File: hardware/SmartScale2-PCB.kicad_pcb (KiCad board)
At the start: 4 copper layers, 42 parts, among them J1 Conn_ARM_JTAG_SWD_10, J2 USB_C_Receptacle_USB2.0_16P, J3 Conn_01x02, J4 Conn_01x06, J5 Conn_01x03_MountingPin, J6 Conn_01x04_MountingPin, Q1 MMBT4403, SW1 SW_Push_JTP-1130, U1 ESP32-C6-WROOM-1, U2 MCP73831-2-OT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

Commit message: PCB rough layout
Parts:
- added L2: L, Inductor_SMD:L_0805_2012Metric_Pad1.05x1.20mm_HandSolder, F.Cu at (45.4, 53.0)
- R12: value R -> 10k
- moved JP1 94.8 mm to (49.5, 50.0), turned to 180 degrees
- moved C11 93.2 mm to (43.2, 53.0), turned to -90 degrees
- moved R10 90.7 mm to (61.2, 61.8)
- moved R11 90.6 mm to (61.2, 63.8)
- moved C12 89.8 mm to (60.2, 55.5)
- moved R8 89.3 mm to (44.8, 63.4)
- moved R9 89.3 mm to (44.8, 60.8)
- moved U3 89.2 mm to (55.1, 58.7)
- moved C10 88.5 mm to (50.1, 62.5)
- moved R6 87.8 mm to (49.4, 57.4)
- moved C9 87.3 mm to (55.1, 65.0)
- moved Q1 87.2 mm to (48.8, 54.5)
- moved J5 85.0 mm to (40.6, 82.2), turned to -90 degrees
- moved JP2 84.5 mm to (63.0, 55.5), turned to -90 degrees
- moved J4 84.4 mm to (38.4, 52.0)
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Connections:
- net Net-(Q1-C) renamed /Q1_C
- J4 pad 3: /A+ -> /A-
- J4 pad 4: /A- -> /A+
- J4 pad 5: /B+ -> /B-
- J4 pad 6: /B- -> /B+
- JP1 pad 1: Net-(JP1-A) -> /Q1_E
- Q1 pad 1: Net-(JP1-A) -> /Q1_B
- Q1 pad 2: Net-(Q1-B) -> /Q1_E
- U1 pad 26: unconnected-(U1-GPIO3/ADC1_CH3-Pad26) -> /T2
- U1 pad 27: unconnected-(U1-GPIO2/ADC1_CH2-Pad27) -> /T1
- U3 pad 1: Net-(JP1-A) -> /Q1_E
- U3 pad 2: Net-(Q1-B) -> /Q1_B
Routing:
- net /B+: track 0.00 -> 29.8 mm
- net /B-: track 0.00 -> 26.6 mm
- net GND: track 0.00 -> 17.5 mm
- net /Q1_C: track 0.00 -> 10.3 mm
- net Net-(U3-INA-): track 0.00 -> 7.29 mm
- net Net-(U3-VFB): track 0.00 -> 7.17 mm
- net Net-(U3-INA+): track 0.00 -> 7.10 mm
- net /A-: track 0.00 -> 7.00 mm
- net /A+: track 0.00 -> 7.00 mm
- net /E+: track 0.00 -> 6.80 mm
- net /RX0: track 0.00 -> 6.74 mm
- net VCC: track 0.00 -> 5.65 mm
- net Net-(U3-VBG): track 0.00 -> 5.61 mm
- net Net-(JP2-C): track 0.00 -> 5.41 mm
- net /Q1_E: track 0.00 -> 3.20 mm
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- added copper zone on In1.Cu, net GND
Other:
- board outline added: 40 x 50 mm
- board text added: "${TITLE} @Jannled"
- board text added: "A+"
- board text added: "A-"
- board text added: "B+"
- board text added: "B-"
- board text added: "E+"
- board text added: "E-"
- board text added: "UART"

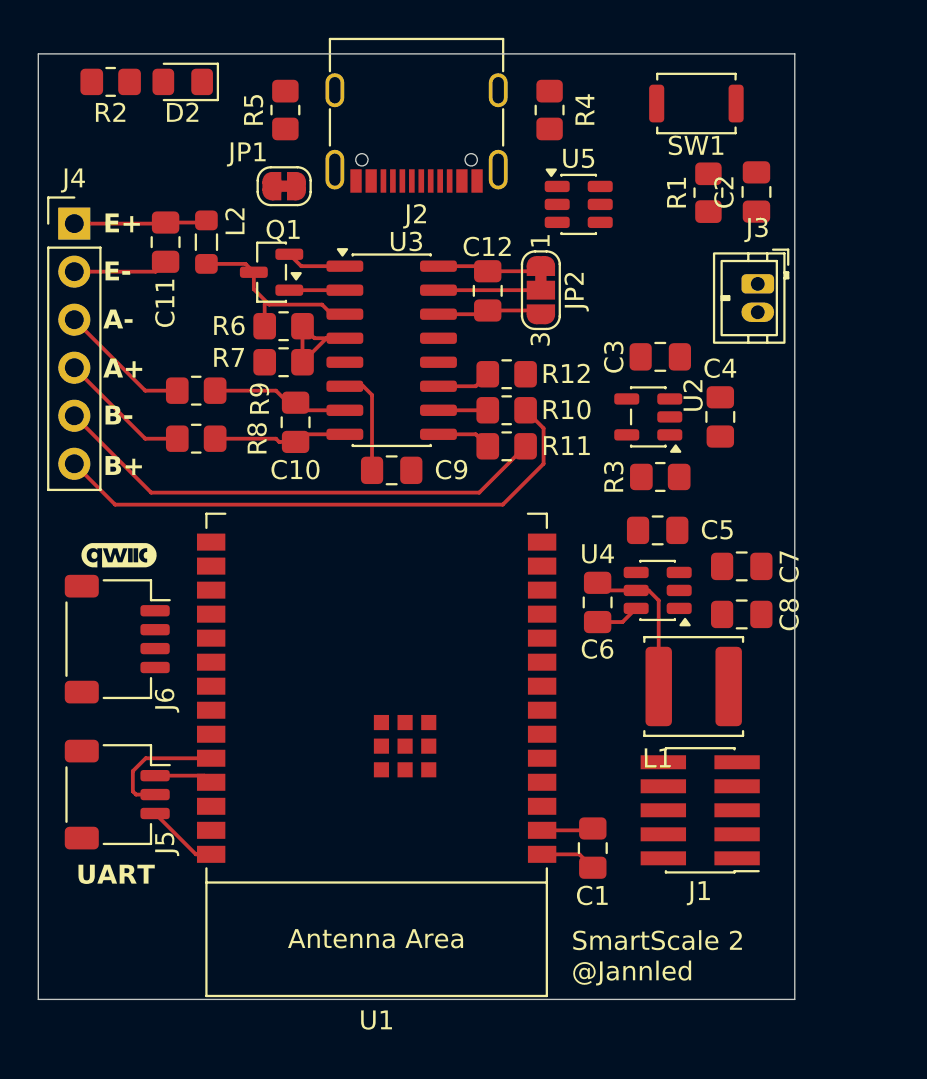
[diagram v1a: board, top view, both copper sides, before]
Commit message: Add Touch IC, continue layout
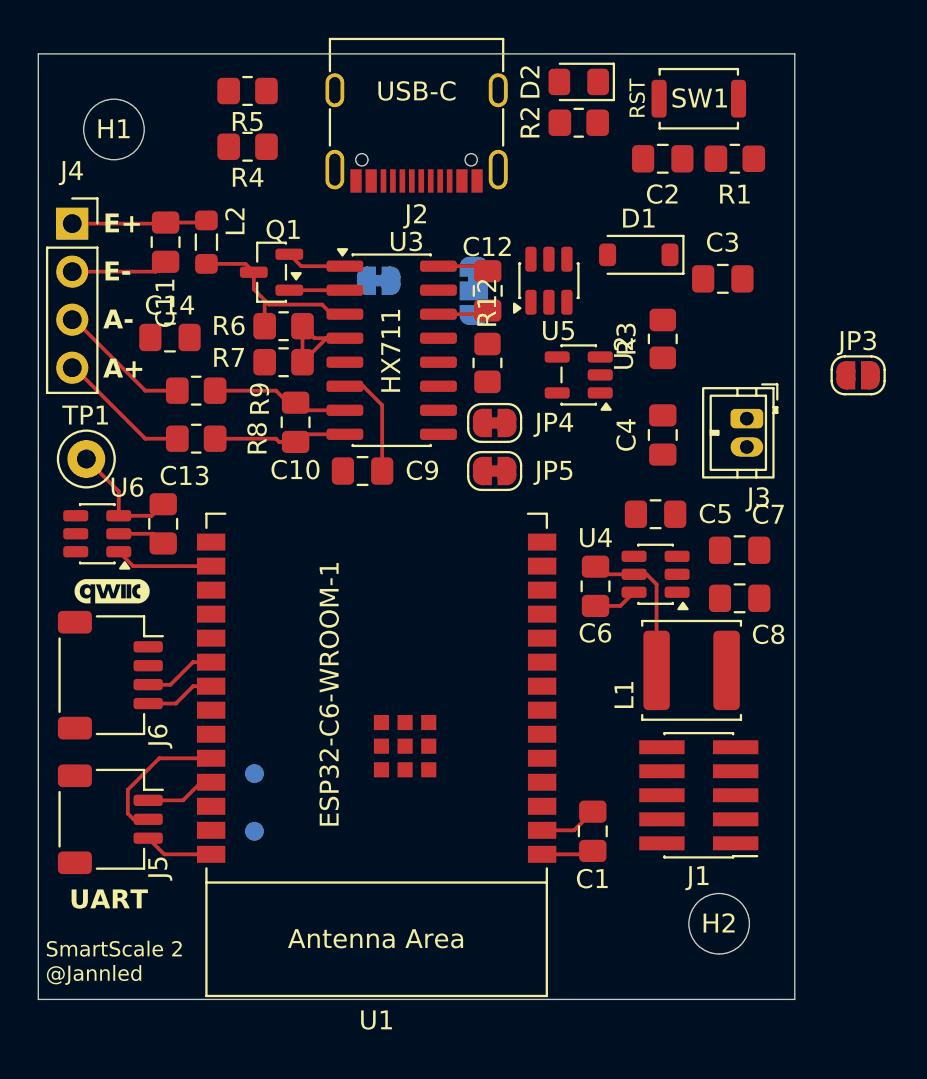
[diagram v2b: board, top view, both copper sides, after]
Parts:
- removed R10, R11: 100, Resistor_SMD:R_0805_2012Metric_Pad1.20x1.40mm_HandSolder
- added C13: 100nF, Capacitor_SMD:C_0805_2012Metric_Pad1.18x1.45mm_HandSolder, F.Cu at (43.1, 67.9)
- added C14: 10uF, Capacitor_SMD:C_0805_2012Metric_Pad1.18x1.45mm_HandSolder, F.Cu at (43.4, 58.0)
- added D1: D_Zener, Diode_SMD:D_SOD-123, F.Cu at (68.2, 53.6)
- added H1: MountingHole, MountingHole:MountingHole_3.2mm_M3_DIN965, F.Cu at (40.5, 47.0)
- added H2: MountingHole, MountingHole:MountingHole_3.2mm_M3_DIN965, F.Cu at (72.5, 89.0)
- added JP3: Jumper_2_Small_Open, Jumper:SolderJumper-2_P1.3mm_Open_RoundedPad1.0x1.5mm, F.Cu at (79.8, 60.0)
- added JP4: Jumper_2_Small_Bridged, Jumper:SolderJumper-2_P1.3mm_Bridged_RoundedPad1.0x1.5mm, F.Cu at (60.6, 62.5)
- added JP5: Jumper_2_Small_Bridged, Jumper:SolderJumper-2_P1.3mm_Bridged_RoundedPad1.0x1.5mm, F.Cu at (60.6, 65.1)
- added TP1: TestPoint, TestPoint:TestPoint_Loop_D2.50mm_Drill1.0mm, F.Cu at (39.0, 64.4)
- added TP2: TestPoint, TestPoint:TestPoint_Pad_D1.0mm, B.Cu at (47.9, 81.1)
- added TP3: TestPoint, TestPoint:TestPoint_Pad_D1.0mm, B.Cu at (47.9, 84.1)
- added U6: ~, Package_TO_SOT_SMD:SOT-23-6, F.Cu at (39.6, 68.4)
- J4: value Conn_01x06 -> Conn_01x04; footprint Connector_PinHeader_2.54mm:PinHeader_1x06_P2.54mm_Vertical -> Connector_PinSocket_2.54mm:PinSocket_1x04_P2.54mm_Vertical
- JP1, JP2: moved to B.Cu
- moved R2 24.8 mm to (65.0, 46.6)
- moved D2 20.9 mm to (65.0, 44.5)
- moved R4 16.1 mm to (47.5, 47.9), turned to 180 degrees
- moved R3 7.30 mm to (69.5, 58.1), turned to 90 degrees
- moved J3 7.15 mm to (73.9, 62.3)
- moved JP1 7.07 mm to (54.5, 55.0), turned to 0 degrees
- moved C3 5.29 mm to (72.7, 54.9)
- moved C2 5.26 mm to (69.5, 48.5), turned to 180 degrees
- moved U5 4.33 mm to (63.5, 55.0), turned to 90 degrees
- moved U2 4.30 mm to (65.0, 60.0)
- moved JP2 3.55 mm to (59.5, 55.5)
- moved C4 3.19 mm to (69.5, 63.2)
- moved R1 2.27 mm to (73.3, 48.5), turned to 180 degrees
- moved R5 2.24 mm to (47.5, 45.0), turned to 180 degrees
- moved G*** 1.94 mm to (40.4, 71.4)
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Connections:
- C2 pad 1: /EN -> /Reset
- R1 pad 2: /EN -> /Reset
- SW1 pad 2: /EN -> /Reset
- U1 pad 11: unconnected-(U1-GPIO10-Pad11) -> /HX711_DOUT
- U1 pad 12: unconnected-(U1-GPIO11-Pad12) -> /HX711_SCK
- U1 pad 16: unconnected-(U1-GPIO18-Pad16) -> /Touch
- U1 pad 20: unconnected-(U1-GPIO22-Pad20) -> /SDA
- U1 pad 21: unconnected-(U1-GPIO23-Pad21) -> /SCL
- U1 pad 26: /T2 -> Net-(U1-GPIO3/ADC1_CH3)
- U1 pad 27: /T1 -> Net-(U1-GPIO2/ADC1_CH2)
- U3 pad 10: Net-(U3-INB+) -> /B+
- U3 pad 9: Net-(U3-INB-) -> /B-
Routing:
- net /B+: track 29.8 -> 0.00 mm
- net /B-: track 26.6 -> 0.00 mm
- net Net-(U6-I): track 0.00 -> 6.31 mm
- net Net-(JP2-C): track 5.41 -> 0.00 mm
- net /Touch: track 0.00 -> 5.20 mm
- net /SDA: track 0.00 -> 3.83 mm
- net /SCL: track 0.00 -> 3.71 mm
- net VCC: track 5.65 -> 2.72 mm
- net Net-(U3-INB-): track 2.87 -> 0.00 mm
- net /HX711_SCK: track 2.87 -> 0.00 mm
- net Net-(U3-INB+): track 2.60 -> 0.00 mm
- net /RX0: track 6.74 -> 7.55 mm
- net GND: track 17.5 -> 16.7 mm
- net /TX0: track 3.11 -> 3.73 mm
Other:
- board text added: "ESP32-C6-WROOM-1"
- board text added: "HX711"
- board text added: "RST"
- board text added: "USB-C"
- board text removed: "B+"
- board text removed: "B-"

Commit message: Push from laptop
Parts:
- JP1: moved to F.Cu
- moved JP1 6.97 mm to (49.2, 50.5)
- moved R3 3.24 mm to (72.7, 57.4), turned to 180 degrees
- moved U5 1.66 mm to (64.4, 53.6)
- moved U2 0.90 mm to (65.7, 59.3)
- moved R4 0.63 mm to (47.5, 47.3)
- moved D1 0.63 mm to (68.8, 53.6), turned to -90 degrees
- moved R5 0.41 mm to (47.5, 45.4)
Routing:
- net /MTDO: track 0.00 -> 13.1 mm
- net /MTCK: track 0.00 -> 12.1 mm, vias 0 -> 2
- net VCC: track 2.72 -> 12.1 mm
- net /MTMS: track 0.00 -> 8.49 mm
- net /MTDI: track 0.00 -> 6.62 mm
- net /Q1_E: track 3.20 -> 6.84 mm
- net /B-: track 0.00 -> 3.12 mm
- net /B+: track 0.00 -> 2.60 mm

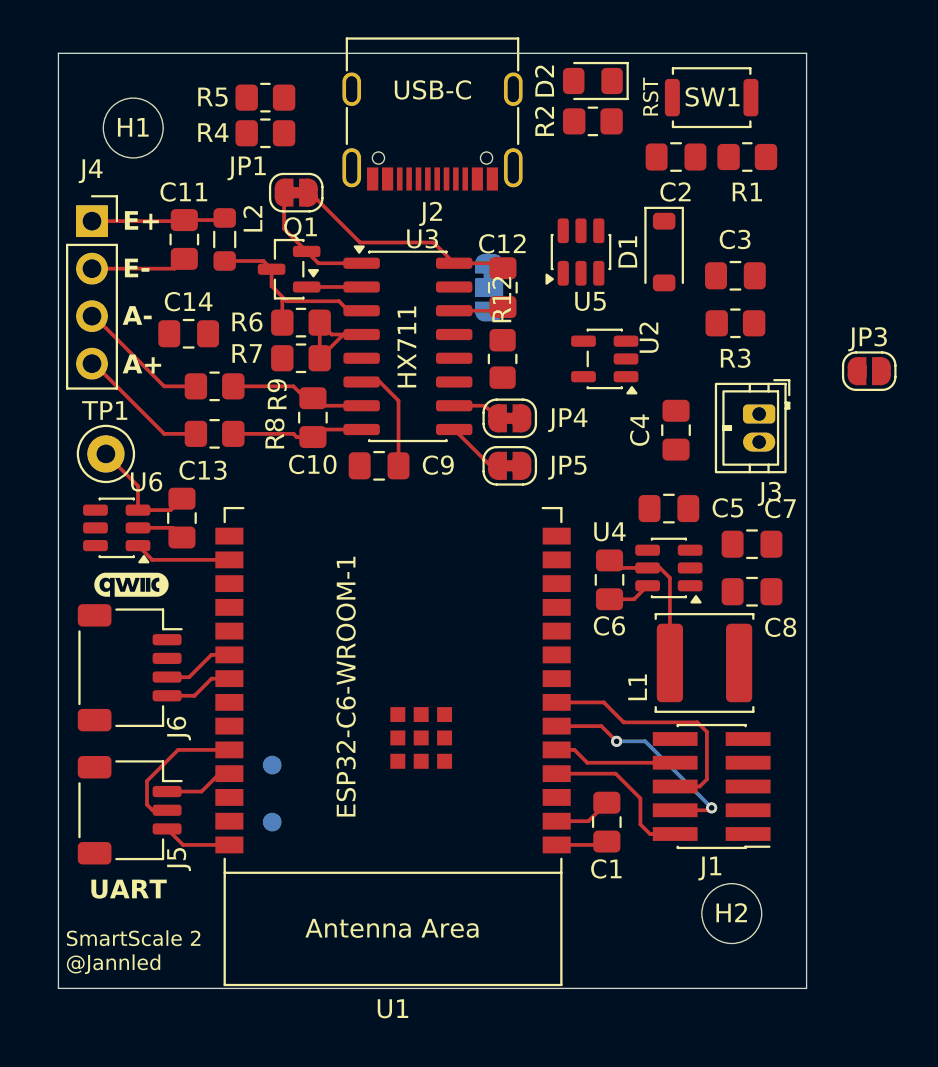
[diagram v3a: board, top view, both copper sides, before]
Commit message: Finish PCB layout
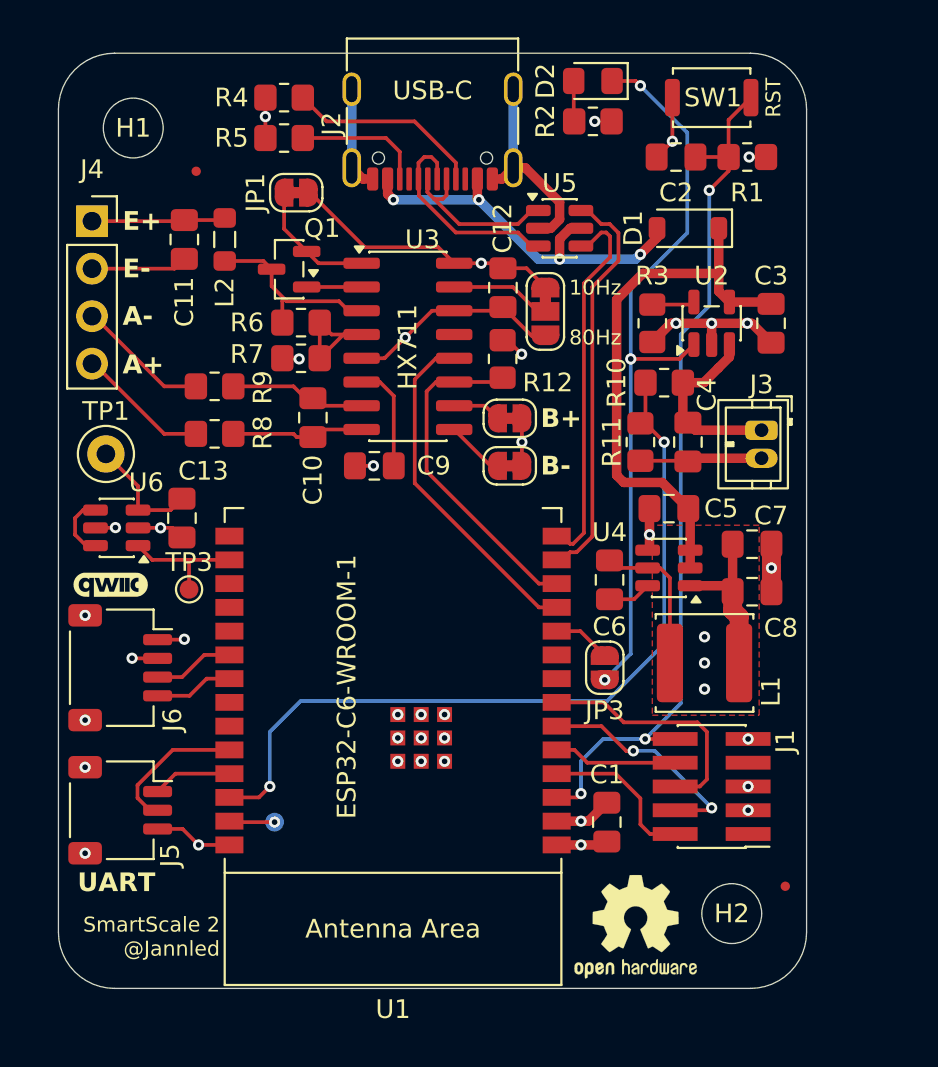
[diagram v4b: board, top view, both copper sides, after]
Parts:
- removed C14: 10uF, Capacitor_SMD:C_0805_2012Metric_Pad1.18x1.45mm_HandSolder
- added FID1: Fiducial, Fiducial:Fiducial_0.5mm_Mask1.5mm, F.Cu at (43.8, 49.3)
- added FID2: Fiducial, Fiducial:Fiducial_0.5mm_Mask1.5mm, F.Cu at (75.3, 87.5)
- added R10: 33k, Resistor_SMD:R_0805_2012Metric_Pad1.20x1.40mm_HandSolder, F.Cu at (68.8, 60.6)
- added R11: 10k, Resistor_SMD:R_0805_2012Metric_Pad1.20x1.40mm_HandSolder, F.Cu at (67.6, 63.8)
- added REF**: OSHW-Logo2_7.3x6mm_SilkScreen, Symbol:OSHW-Logo2_7.3x6mm_SilkScreen, F.Cu at (67.3, 89.7)
- JP2, TP3: moved to F.Cu
- moved JP3 21.2 mm to (65.7, 75.9), turned to -90 degrees
- moved TP3 13.2 mm to (43.5, 71.7), turned to 0 degrees
- moved U2 6.02 mm to (71.4, 57.4), turned to 90 degrees
- moved R3 4.44 mm to (68.2, 57.4), turned to -90 degrees
- moved JP2 3.26 mm to (62.5, 56.8)
- moved C3 3.18 mm to (74.6, 57.4), turned to 90 degrees
- moved TP2 3.05 mm to (48.0, 84.1)
- moved R5 2.38 mm to (48.5, 47.5)
- moved R4 2.15 mm to (48.5, 45.4)
- moved D1 1.80 mm to (70.1, 52.4), turned to 180 degrees
- moved U5 1.71 mm to (63.3, 52.4), turned to 0 degrees
- moved G*** 1.11 mm to (39.3, 71.4)
- moved C4 0.90 mm to (70.1, 63.8)
- moved J3 0.87 mm to (74.1, 63.2)
- moved J5 0.51 mm to (39.8, 83.5)
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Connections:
- net Net-(J3-Pin_1) renamed +BATT
- C1 pad 2: +3.3V -> +3V3
- C12 pad 1: VCC -> +3V3
- J6 pad 2: +3.3V -> +3V3
- JP1 pad 2: VCC -> +3V3
- JP2 pad 1: VCC -> +3V3
- JP3 pad 1: unconnected-(JP3-A-Pad1) -> Net-(JP3-A)
- R12 pad 1: VCC -> +3V3
- R2 pad 2: VCC -> +3V3
- TP3 pad 1: Net-(U1-GPIO3/ADC1_CH3) -> /Touch
- U1 pad 10: unconnected-(U1-GPIO8-Pad10) -> Net-(JP3-A)
- U1 pad 2: +3.3V -> +3V3
- U1 pad 26: Net-(U1-GPIO3/ADC1_CH3) -> /VBat_Div
- U3 pad 16: VCC -> +3V3
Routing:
- net GND: track 16.7 -> 74.0 mm, vias 0 -> 31
- net /Reset: track 0.00 -> 47.1 mm, vias 0 -> 3
- net /VBat_Div: track 0.00 -> 43.1 mm, vias 0 -> 2
- net /LED_CHRG: track 0.00 -> 39.9 mm, vias 0 -> 3
- net +3V3: track 0.00 -> 32.3 mm, vias 0 -> 10
- net /USB_-: track 0.00 -> 21.7 mm
- net Net-(D1-A): track 0.00 -> 21.2 mm, vias 0 -> 4
- net /USB_+: track 0.00 -> 20.2 mm
- net /HX711_DOUT: track 0.00 -> 18.5 mm
- net /HX711_SCK: track 0.00 -> 18.1 mm
- net VCC: track 12.1 -> 29.7 mm
- net /USB_ESD_P: track 0.00 -> 11.4 mm
- net Net-(J2-CC1): track 0.00 -> 10.5 mm
- net +BATT: track 0.00 -> 10.1 mm
- net /USB_ESD_N: track 0.00 -> 9.27 mm
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- added copper zone on F.Cu, net +3V3
- added copper zone on In2.Cu, net +3V3
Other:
- outline, holes or cut-outs redrawn
- board text added: "B+"
- board text added: "B-"

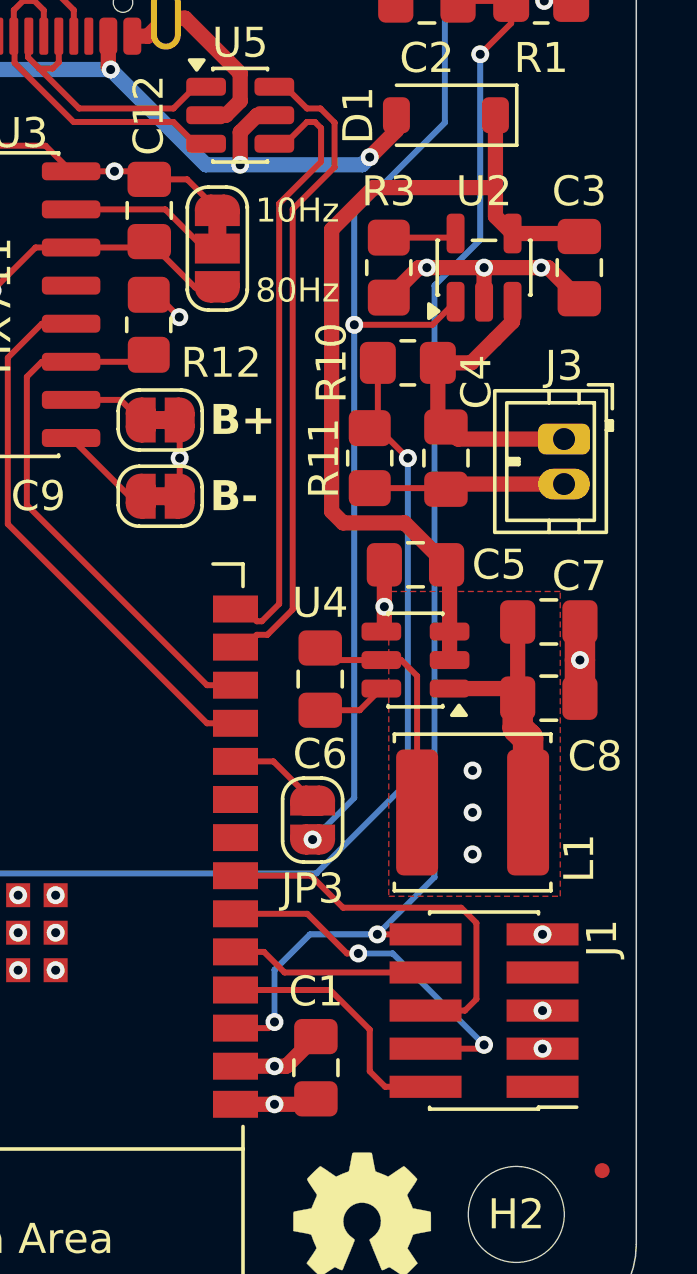
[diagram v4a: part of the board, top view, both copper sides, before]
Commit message: Change inductor, add pin labels
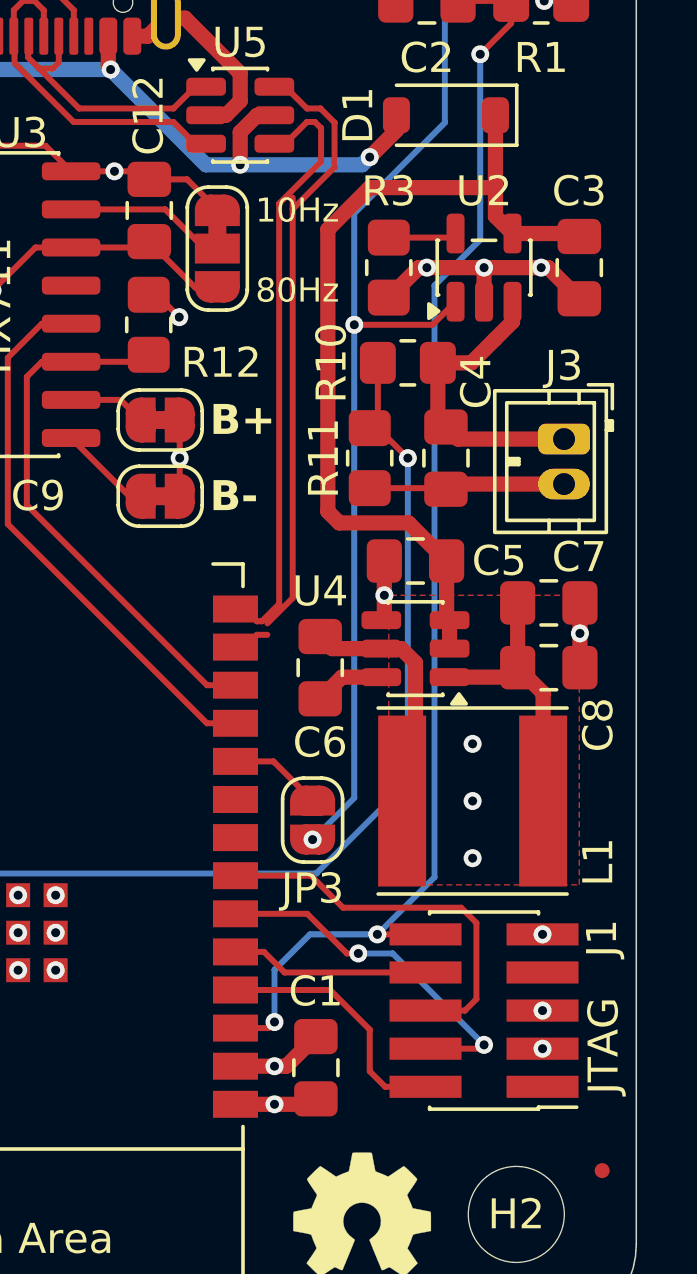
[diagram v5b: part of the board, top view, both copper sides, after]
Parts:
- L1: footprint Inductor_SMD:L_Sunlord_SWPA5040S -> Inductor_SMD:L_Taiyo-Yuden_NR-60xx
- L2: value L -> 3.3uH
- U6: value ~ -> TTP223-BA6
- moved C8 1.02 mm to (73.5, 70.8)
- moved C7 0.64 mm to (73.5, 68.6)
- moved C6 0.38 mm to (65.9, 70.8)
- moved L1 0.38 mm to (71.0, 75.2)
- moved U4 0.38 mm to (69.1, 70.1)
- moved C5 0.13 mm to (69.1, 67.2)
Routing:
- net GND: track 74.0 -> 73.4 mm
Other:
- board text added: "JTAG"

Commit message: Finish PCB
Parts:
- D1: value D_Zener -> BZT52C12
- J3: footprint Connector_JST:JST_ZH_B2B-ZR_1x02_P1.50mm_Vertical -> Connector_Molex:Molex_PicoBlade_53047-0210_1x02_P1.25mm_Vertical
- R1: value 12k -> 10k
- moved J3 0.71 mm to (73.3, 63.2)
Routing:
- net +BATT: track 10.1 -> 9.37 mm
- net GND: track 73.4 -> 72.8 mm
